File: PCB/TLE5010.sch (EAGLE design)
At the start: 10 parts, among them U1 TLE5010

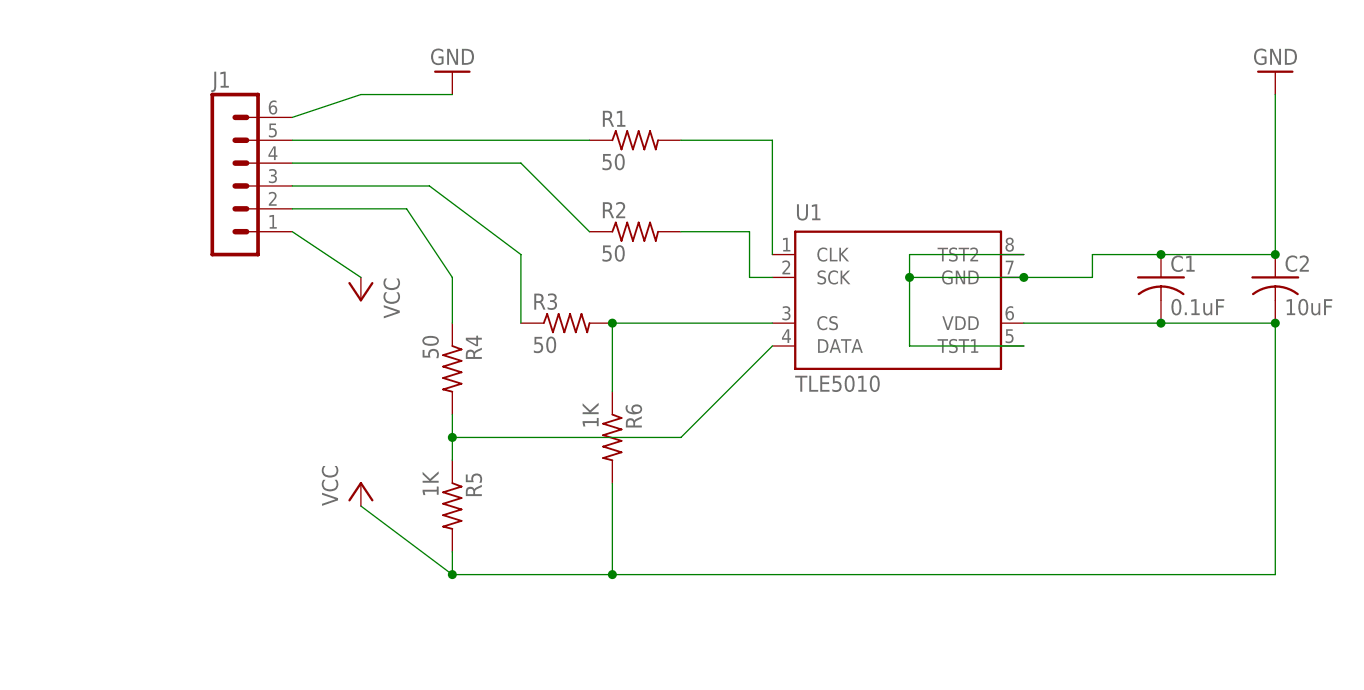
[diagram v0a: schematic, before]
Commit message: Fixed J1 orientation
now corresponds with Cougar MMjoy board headers
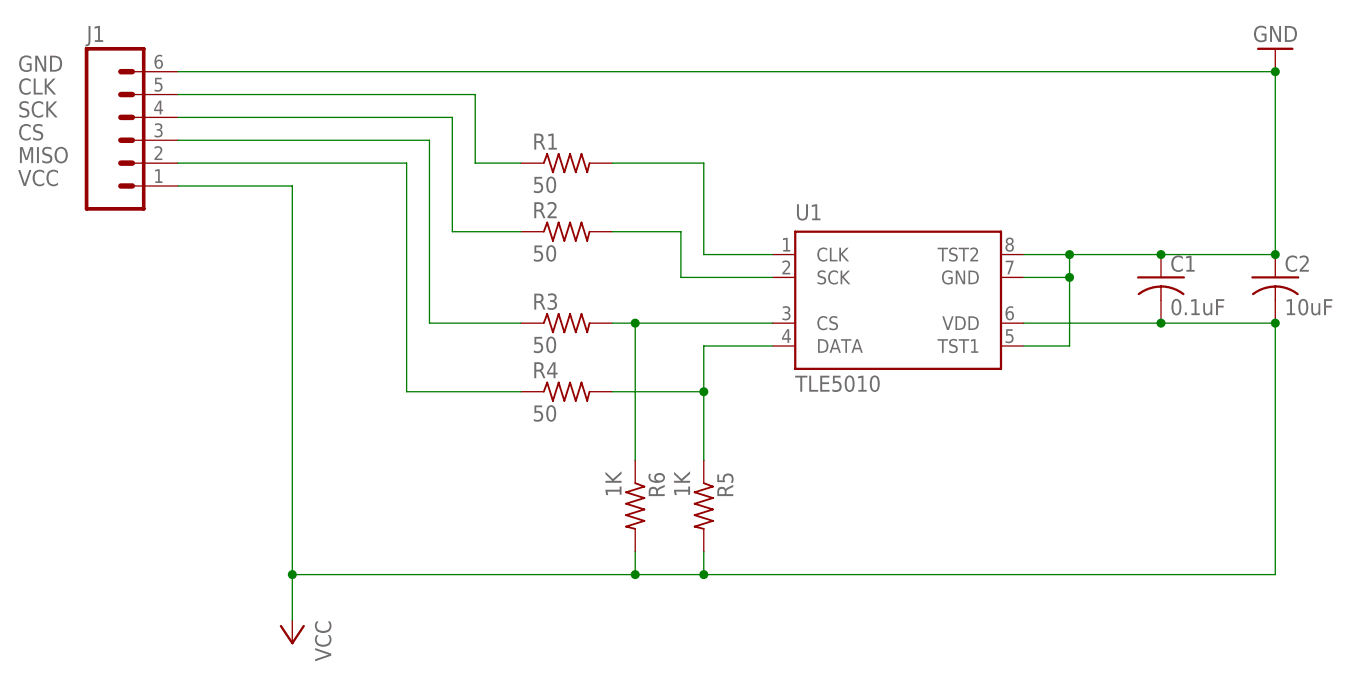
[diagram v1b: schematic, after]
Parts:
- J1: device con-lstb:MA06-1 -> SparkFun-Connectors:M06POLAR_LOCK
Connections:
- net N$11 renamed MISO
- net N$3 renamed CLK
- net N$4 renamed SCK
- net N$5 renamed CS
- net N$7 renamed DATA
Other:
- moved on the sheet: R1, R2, R4, R5, R6
